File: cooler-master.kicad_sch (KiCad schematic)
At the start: 2 parts, among them Q1 G040P04M, U1 STM32G473CBT3

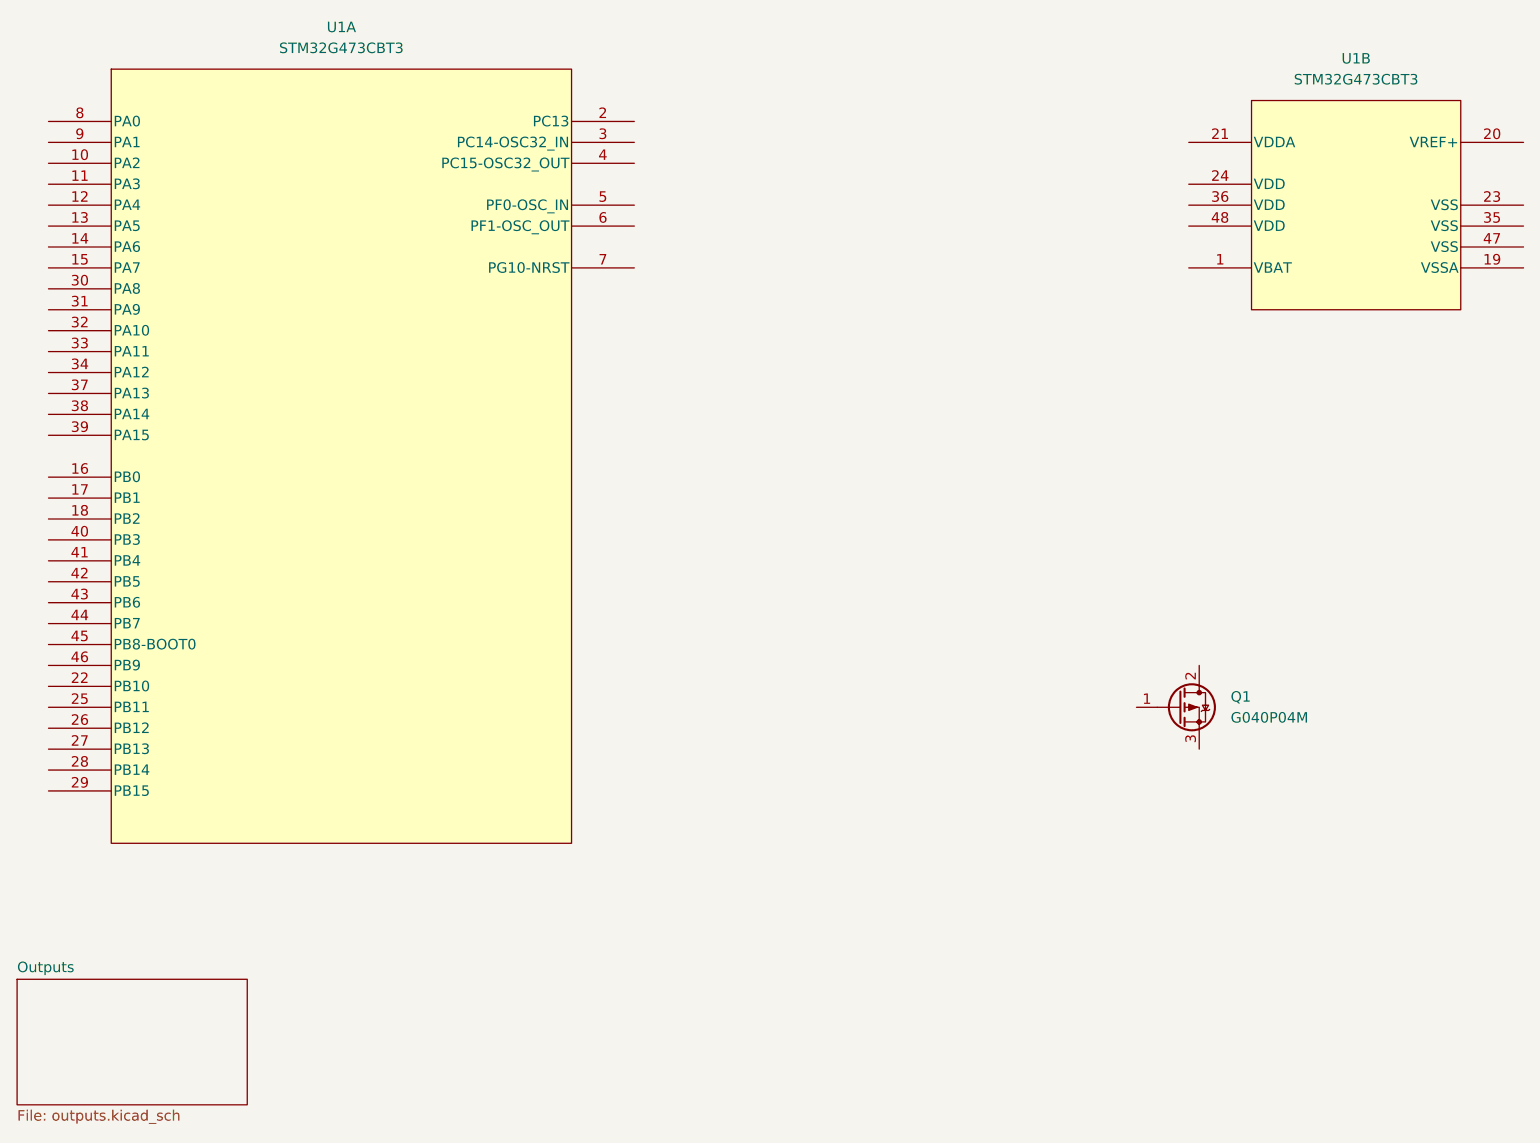
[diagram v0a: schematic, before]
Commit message: More sheets and switching to external FET HSS
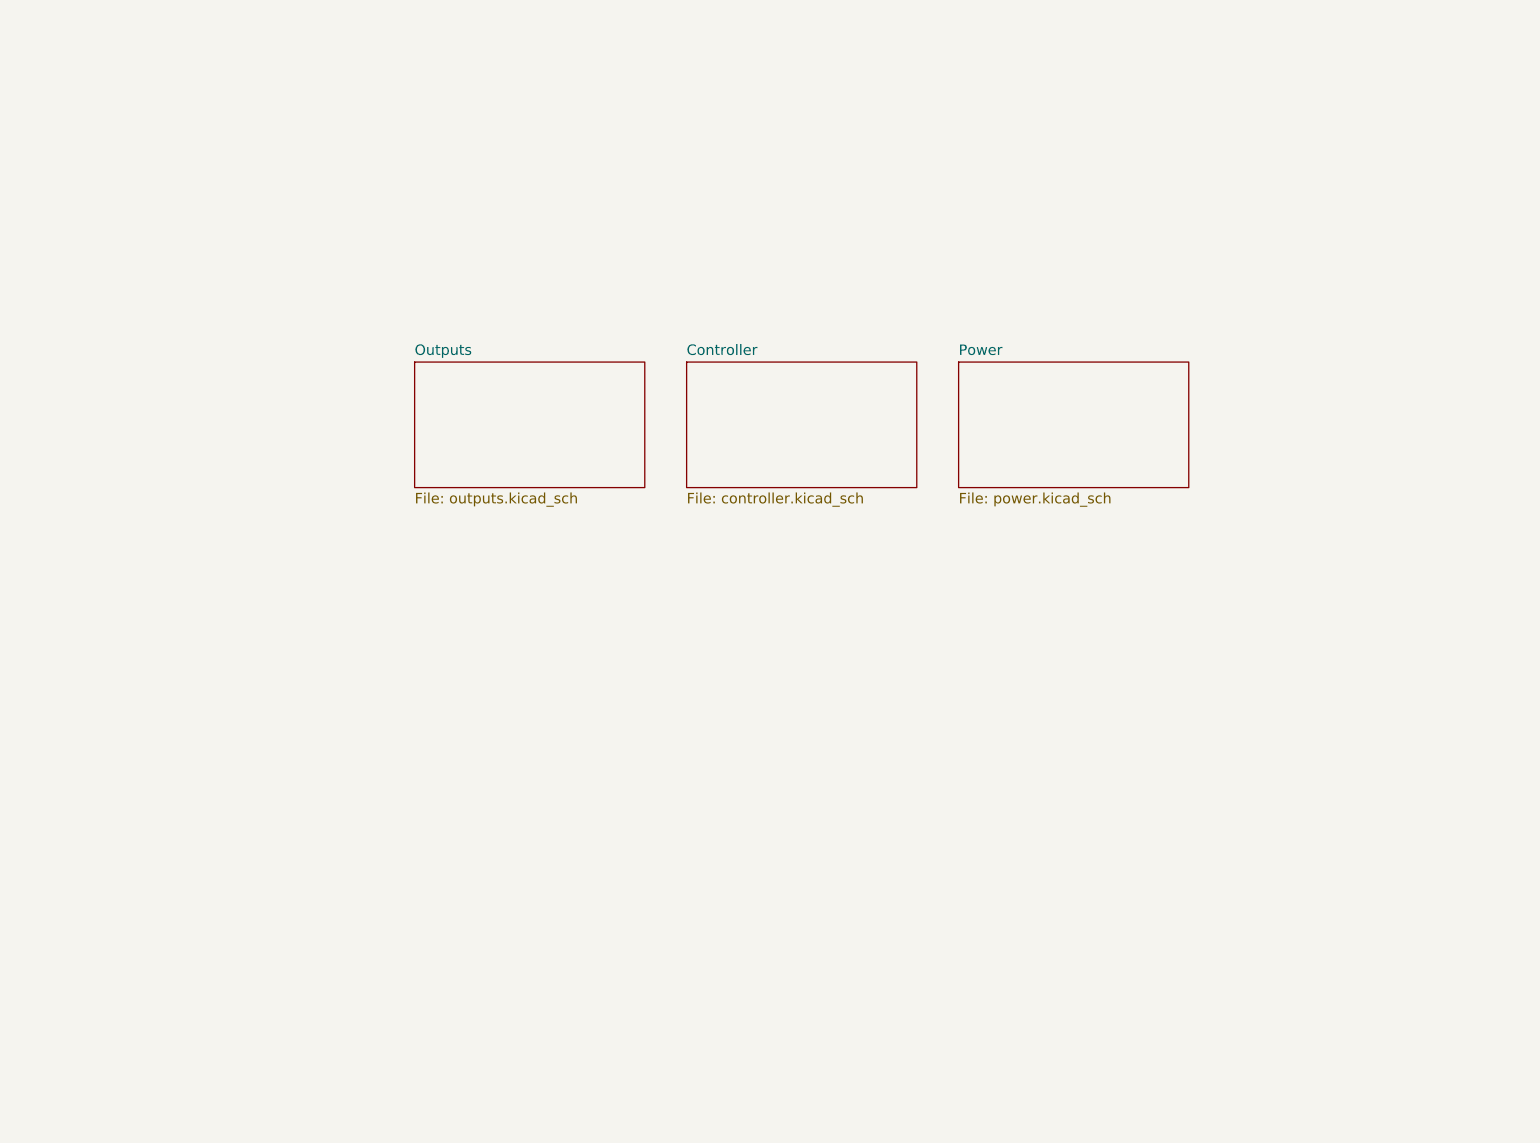
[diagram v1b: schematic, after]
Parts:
- removed Q1: G040P04M, Sullivan-Labs:TO-263-3, D2PAK, symbol Sullivan-Labs:PMOS G040P04M
- removed U1: STM32G473CBT3, Sullivan-Labs:LQFP48-7x7mm, symbol Sullivan-Labs:MCU STM32G473
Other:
- added sheet Controller (controller.kicad_sch)
- added sheet Power (power.kicad_sch)

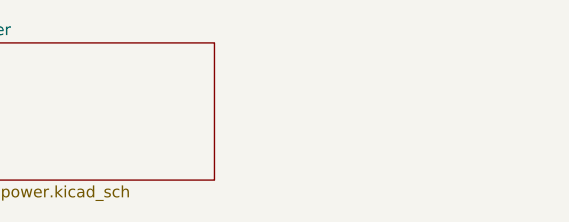
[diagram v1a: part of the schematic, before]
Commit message: Added peripherals page and started gauge control
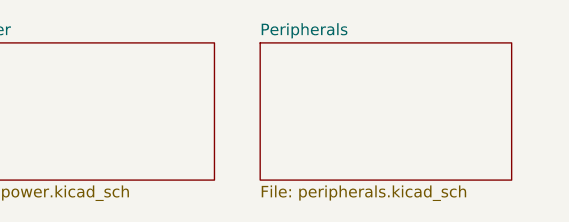
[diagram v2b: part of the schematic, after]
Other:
- added sheet Peripherals (peripherals.kicad_sch)
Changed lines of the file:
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@@
 	(paper "A4")
+	(sheet
+		(at 199.39 78.74)
+		(size 27.94 15.24)
+		(fields_autoplaced yes)
+		(stroke
+			(width 0.1524)
+			(type solid)
+		)
+		(fill
+			(color 0 0 0 0.0000)
+		)
+		(property "Sheetname" "Peripherals"
+			(at 199.39 78.0284 0)
+			(effects
+				(font
+					(size 1.27 1.27)
+				)
+				(justify left bottom)
+			)
+		)
+		(property "Sheetfile" "peripherals.kicad_sch"
+			(at 199.39 94.5646 0)
+			(effects
+				(font
+					(size 1.27 1.27)
+				)
+				(justify left top)
+			)
+		)
+		(instances
+			(project "cooler-master"
+				(path "/d013d610-c58f-4b11-9d18-37fc135ac516"
+					(page "5")
+				)
+			)
+		)
+	)
 	(sheet
 		(at 166.37 78.74)
